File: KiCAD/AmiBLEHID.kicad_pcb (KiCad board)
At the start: 2 copper layers, 31 x 33.5 mm, 7 parts, among them J1 D-Sub Female, SW1 Reset, SW2 Mode, U1 ESP32-H2-Zero, U2 74HC05

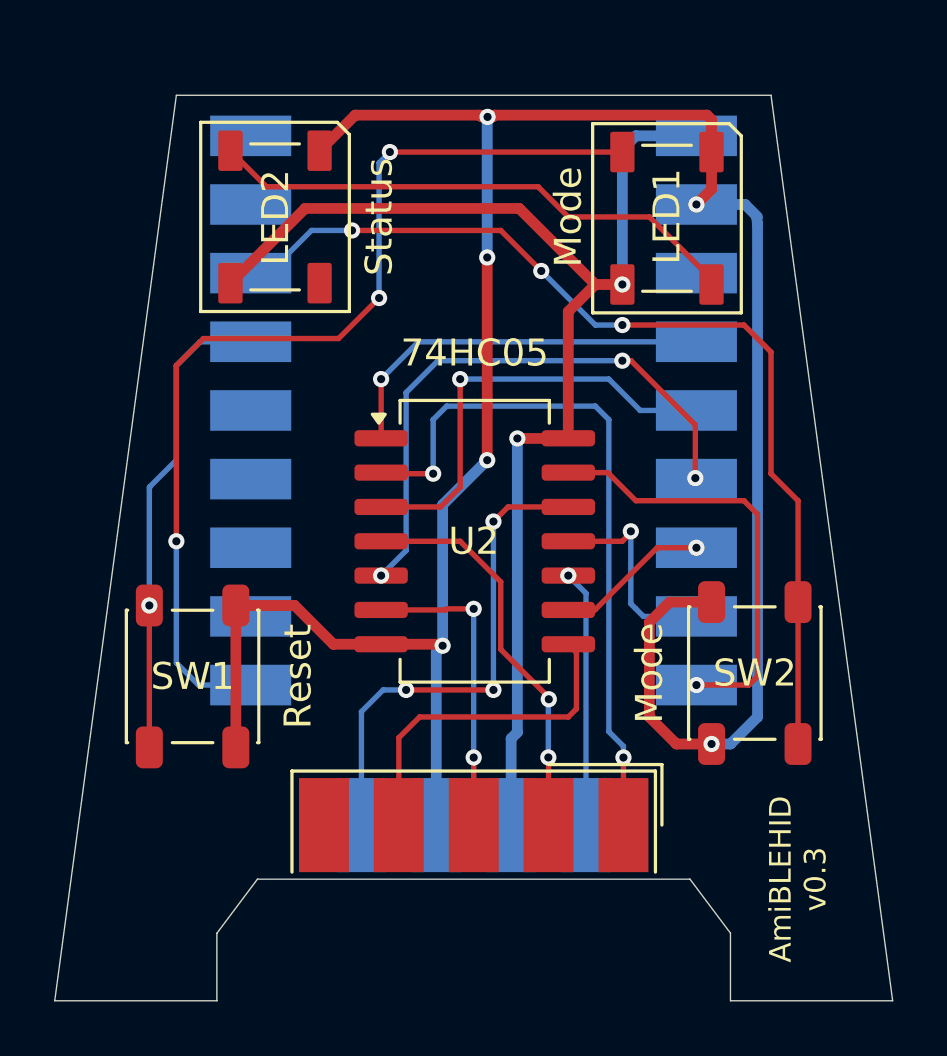
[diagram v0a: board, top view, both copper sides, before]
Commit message: WIP - Updates for new iteration with WS2812 LEDs
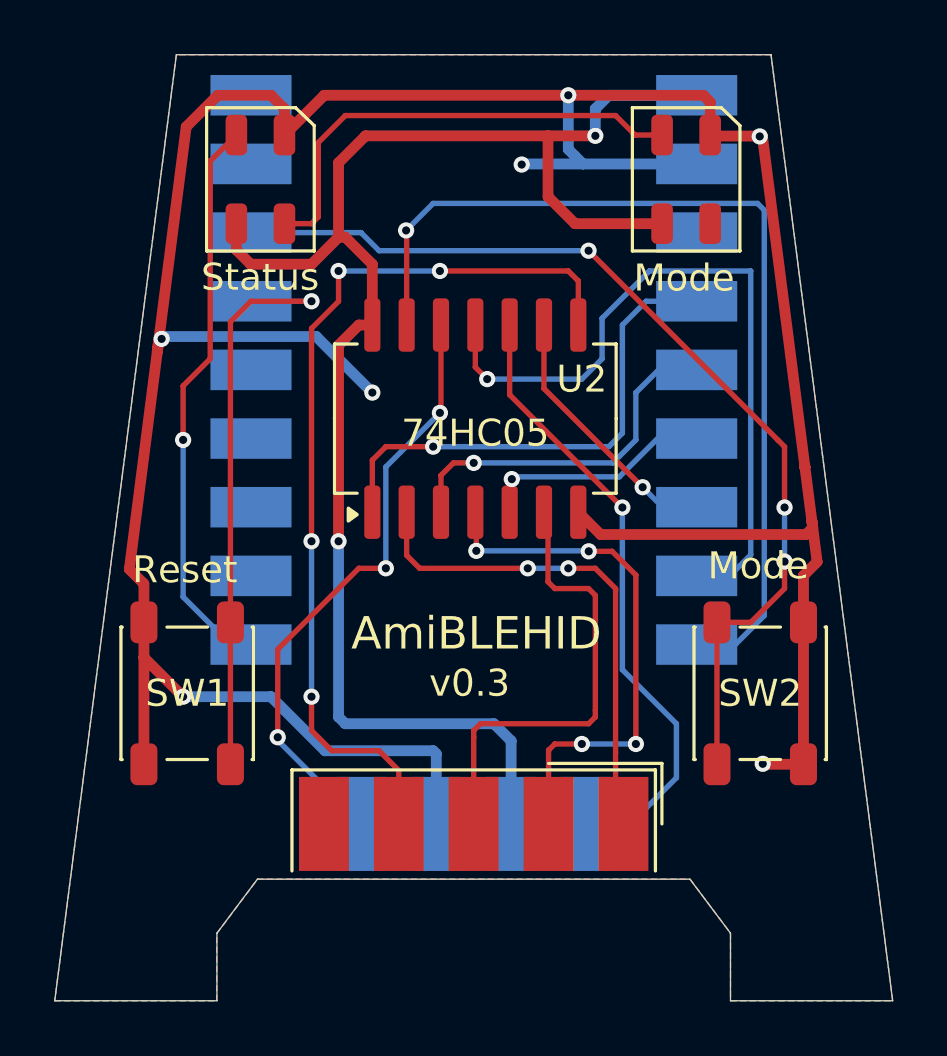
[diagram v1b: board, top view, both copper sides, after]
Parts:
- Mode: renamed from LED2; footprint LED_SMD:LED_WS2812B_PLCC4_5.0x5.0mm_P3.2mm -> LED_SMD:LED_WS2812B-Mini_PLCC4_3.5x3.5mm
- Status: renamed from LED1; footprint LED_SMD:LED_WS2812B_PLCC4_5.0x5.0mm_P3.2mm -> LED_SMD:LED_WS2812B-Mini_PLCC4_3.5x3.5mm
- moved Mode 15.3 mm to (102.9, 42.1)
- moved Status 15.1 mm to (87.1, 42.1)
- moved U2 4.54 mm to (95.1, 51.0), turned to 90 degrees
- moved U1 1.50 mm to (95.5, 48.9)
- moved SW2 0.78 mm to (105.6, 61.1), turned to 90 degrees
- moved SW1 0.66 mm to (84.4, 61.1), turned to -90 degrees
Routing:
- net GND: track 91.0 -> 116.9 mm, vias 6 -> 7
- net Net-(J1-Pad4): track 12.9 -> 33.9 mm, vias 0 -> 4
- net Net-(U1-IO4): track 7.80 -> 27.3 mm
- net Net-(U1-IO5): track 16.0 -> 35.2 mm
- net Net-(LED1-DIN): track 36.8 -> 21.1 mm, vias 3 -> 1
- net Net-(J1-Pad6): track 9.60 -> 23.4 mm
- net Net-(J1-Pad1): track 26.2 -> 12.7 mm
- net Net-(U1-IO2): track 21.3 -> 8.72 mm, vias 3 -> 1
- net +5V: track 47.1 -> 58.9 mm
- net Net-(J1-Pad3): track 11.5 -> 3.16 mm, vias 2 -> 0
- net Net-(J1-Pad2): track 14.9 -> 20.0 mm, vias 2 -> 4
- net Net-(SW1-A): track 17.7 -> 22.7 mm
- net Net-(U1-IO3): track 5.69 -> 10.0 mm
- net Net-(U1-IO0): track 14.4 -> 18.7 mm
- net Net-(J1-Pad9): track 18.7 -> 22.8 mm
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- added copper zone on B.Cu, net GND
- added copper zone on F.Cu, net GND
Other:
- board size 31 x 33.5 mm -> 31 x 35 mm
- board text added: "1 +5V"
- board text added: "10"
- board text added: "18"
- board text added: "2 GND"
- board text added: "9"
- board text added: "AmiBLEHID"
- board text added: "v0.3"
- board text removed: "AmiBLEHID v0.3"

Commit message: KiCAD project updates - *untested* 0.4 revision aimed at enabling CD32 protocol support
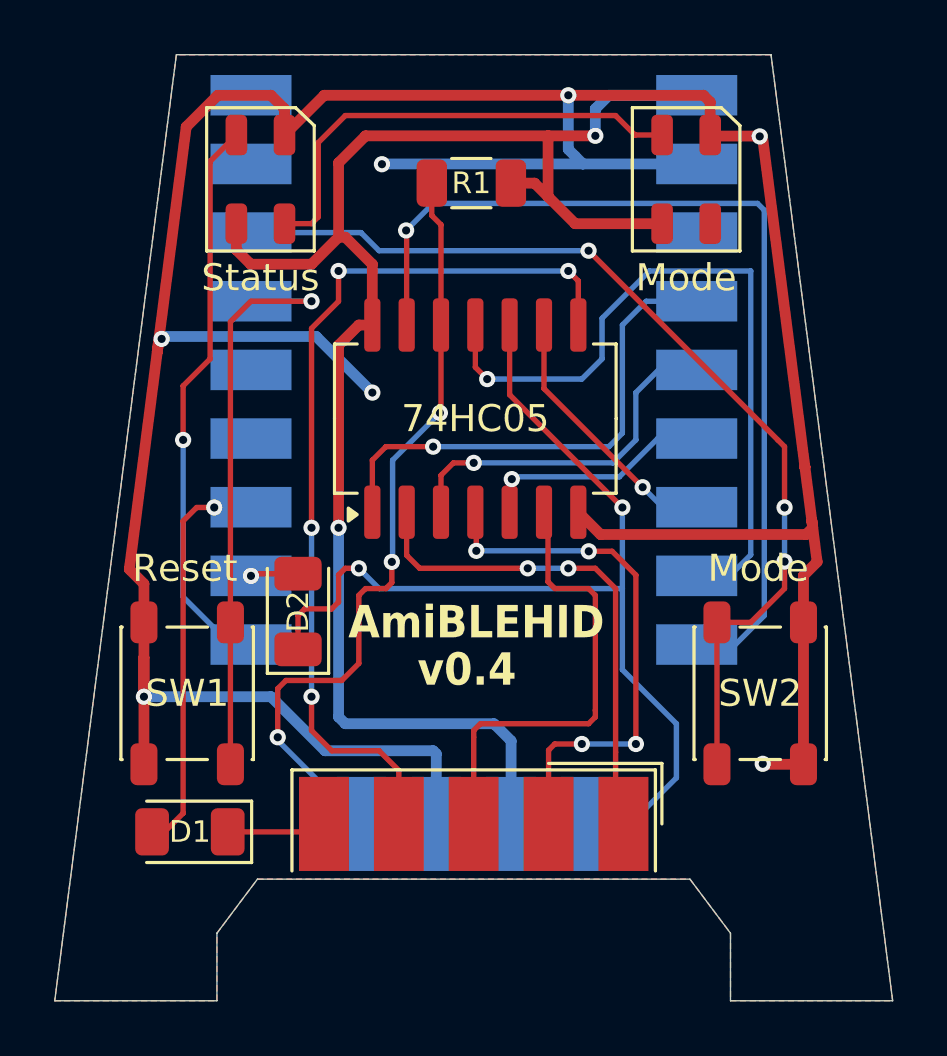
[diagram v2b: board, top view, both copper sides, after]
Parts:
- added D1: 1N4148, Diode_SMD:D_1206_3216Metric, F.Cu at (84.5, 66.2)
- added D2: 1N4148, Diode_SMD:D_1206_3216Metric, F.Cu at (88.5, 58.1)
- added R1: 470, Resistor_SMD:R_1206_3216Metric, F.Cu at (94.9, 42.2)
- renumbered Status to LED1, Mode to LED2
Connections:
- net Net-(J1-Pad1) renamed J_UP
- net Net-(J1-Pad2) renamed J_DOWN
- net Net-(J1-Pad3) renamed J_LEFT
- net Net-(J1-Pad4) renamed J_RIGHT
- net Net-(J1-Pad6) renamed J_FIRE
- net Net-(J1-Pad9) renamed J_POTX
- J1 pad 5: unconnected-(J1-Pad5) -> J_POTY
- U1 pad 11: unconnected-(U1-IO11-Pad11) -> Net-(D2-A)
- U1 pad 12: unconnected-(U1-IO12-Pad12) -> Net-(D1-A)
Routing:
- net J_FIRE: track 23.4 -> 37.5 mm, vias 1 -> 2
- net Net-(D1-A): track 0.00 -> 13.1 mm, vias 0 -> 1
- net J_POTX: track 22.8 -> 29.3 mm
- net GND: track 116.9 -> 122.9 mm
- net J_POTY: track 0.00 -> 4.14 mm
- net Net-(D2-A): track 0.00 -> 1.77 mm, vias 0 -> 1
- net +5V: track 58.9 -> 60.5 mm
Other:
- board text added: "v0.4"
- board text removed: "v0.3"
